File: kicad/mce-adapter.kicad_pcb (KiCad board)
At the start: 2 copper layers, 64.8 x 36.8 mm, 18 parts, among them U1 GAL16V8

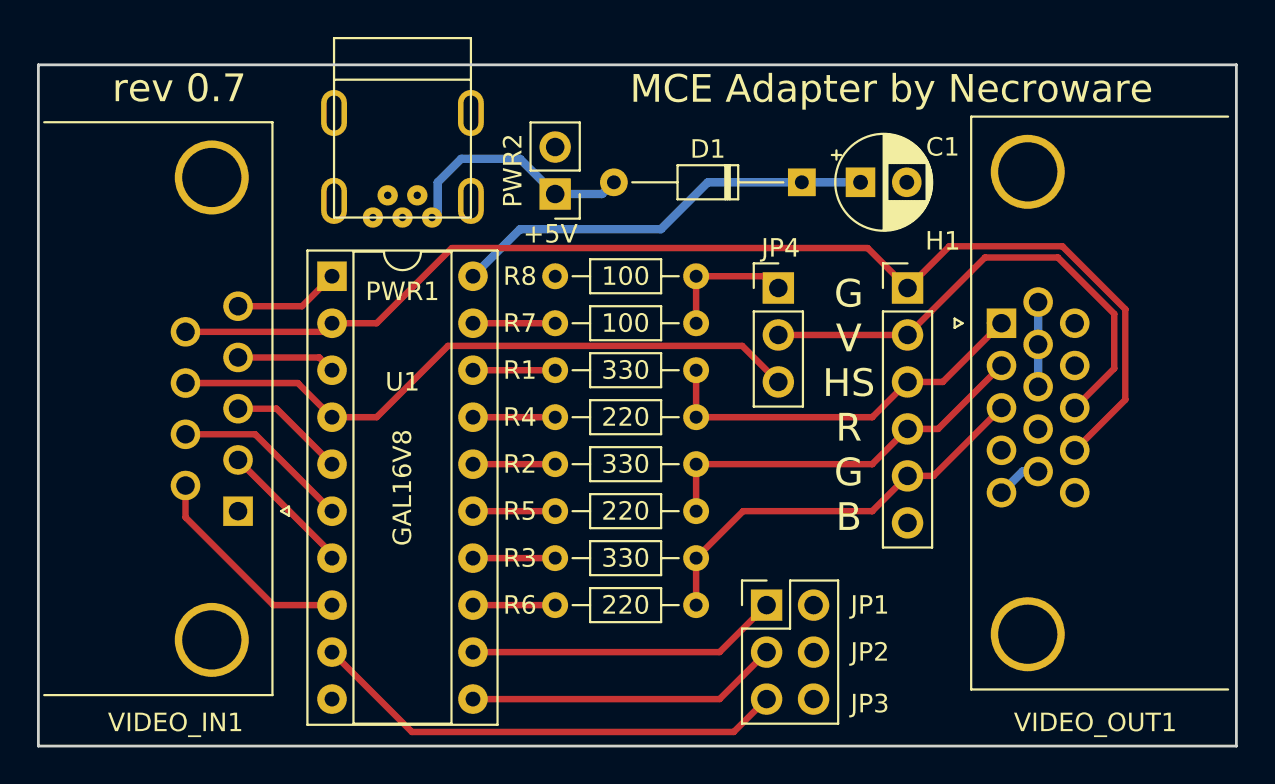
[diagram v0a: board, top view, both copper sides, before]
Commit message: Vastly shrink PCB
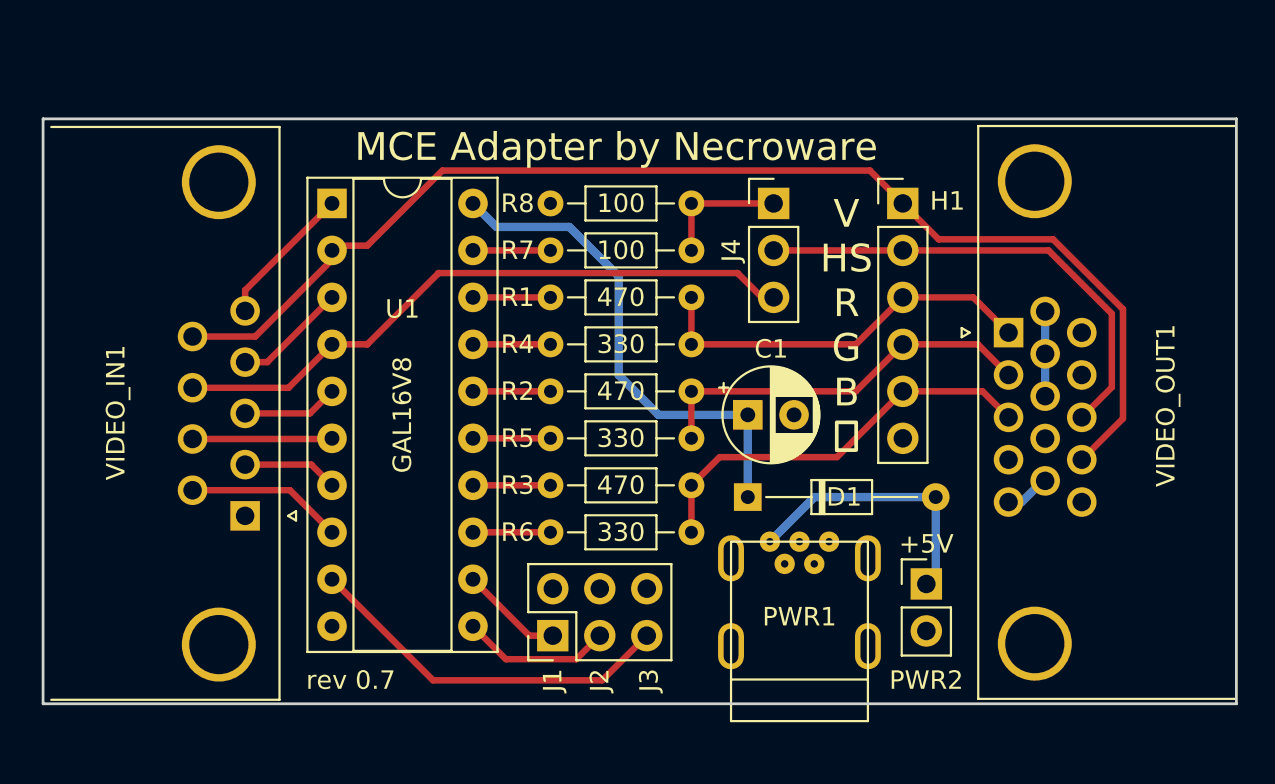
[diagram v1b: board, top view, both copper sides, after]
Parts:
- removed JP1-3: Conn_02x03_Odd_Even, Connector_PinHeader_2.54mm:PinHeader_2x03_P2.54mm_Vertical
- removed JP4: Conn_01x03_Male, Connector_PinHeader_2.54mm:PinHeader_1x03_P2.54mm_Vertical
- added J123: Conn_02x03_Odd_Even, Connector_PinHeader_2.54mm:PinHeader_2x03_P2.54mm_Vertical, F.Cu at (138.3, 114.7)
- added J4: Conn_01x03_Male, Connector_PinHeader_2.54mm:PinHeader_1x03_P2.54mm_Vertical, F.Cu at (150.2, 91.3)
- R1, R2, R3: value 330 -> 470
- R4, R5, R6: value 220 -> 330
- moved PWR2 29.1 mm to (158.5, 111.9), turned to 0 degrees
- moved PWR1 27.7 mm to (151.6, 109.6), turned to 0 degrees
- moved D1 17.3 mm to (148.8, 107.2), turned to 0 degrees
- moved C1 14.0 mm to (148.8, 102.7)
- moved H1 4.58 mm to (157.2, 91.3)
- moved R7 3.95 mm to (145.8, 93.9)
- moved R1 3.95 mm to (145.8, 96.4)
- moved R2 3.95 mm to (145.8, 101.5)
- moved R3 3.95 mm to (145.8, 106.6)
- moved R4 3.95 mm to (145.8, 98.9)
- moved R5 3.95 mm to (145.8, 104.0)
- moved R6 3.95 mm to (145.8, 109.1)
- moved R8 3.95 mm to (145.8, 91.3)
- moved U1 3.94 mm to (126.4, 91.3)
- moved VIDEO_OUT1 0.63 mm to (162.9, 98.3)
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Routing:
- net SW1_IN: track 16.9 -> 5.58 mm
- net SW2_IN: track 16.9 -> 8.12 mm
- net SW3_IN: track 26.0 -> 20.3 mm
- net Net-(C1-Pad1): track 23.1 -> 27.8 mm
- net IG_IN: track 11.6 -> 8.48 mm
- net Net-(D1-Pad2): track 13.1 -> 15.5 mm
- net IR_IN: track 7.41 -> 5.16 mm
- net IB_IN: track 9.78 -> 7.55 mm
- net B_IN: track 5.75 -> 7.76 mm
- net V_IN: track 65.0 -> 66.1 mm
- net R_IN: track 6.32 -> 5.19 mm
- net G_IN: track 5.37 -> 6.15 mm
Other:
- board size 64.8 x 36.8 mm -> 64.5 x 31.6 mm
- board text added: "V HS R G B ⏚"
- board text removed: "G V HS R G B"

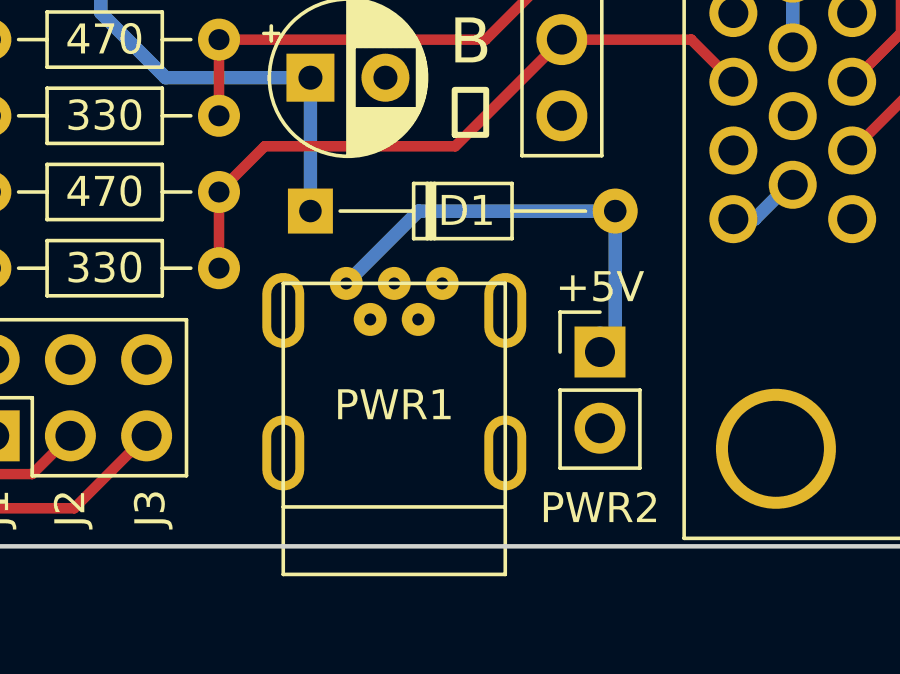
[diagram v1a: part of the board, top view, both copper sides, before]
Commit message: Move USB slightly over the edge
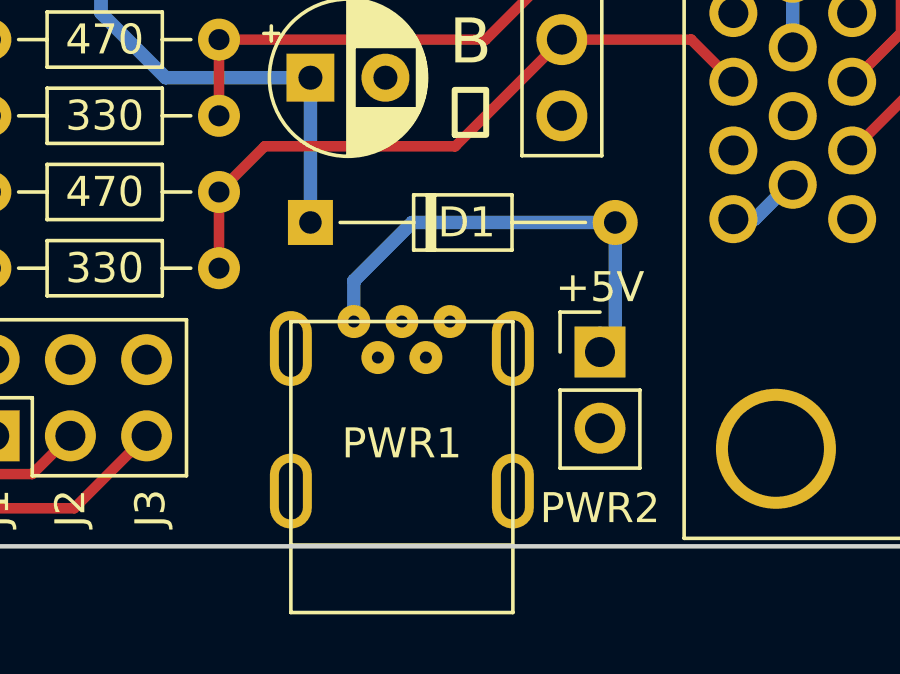
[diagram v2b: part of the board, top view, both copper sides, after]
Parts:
- moved PWR1 1.30 mm to (151.9, 110.9)
- moved D1 0.38 mm to (148.8, 107.6)
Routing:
- net Net-(D1-Pad2): track 15.5 -> 16.0 mm

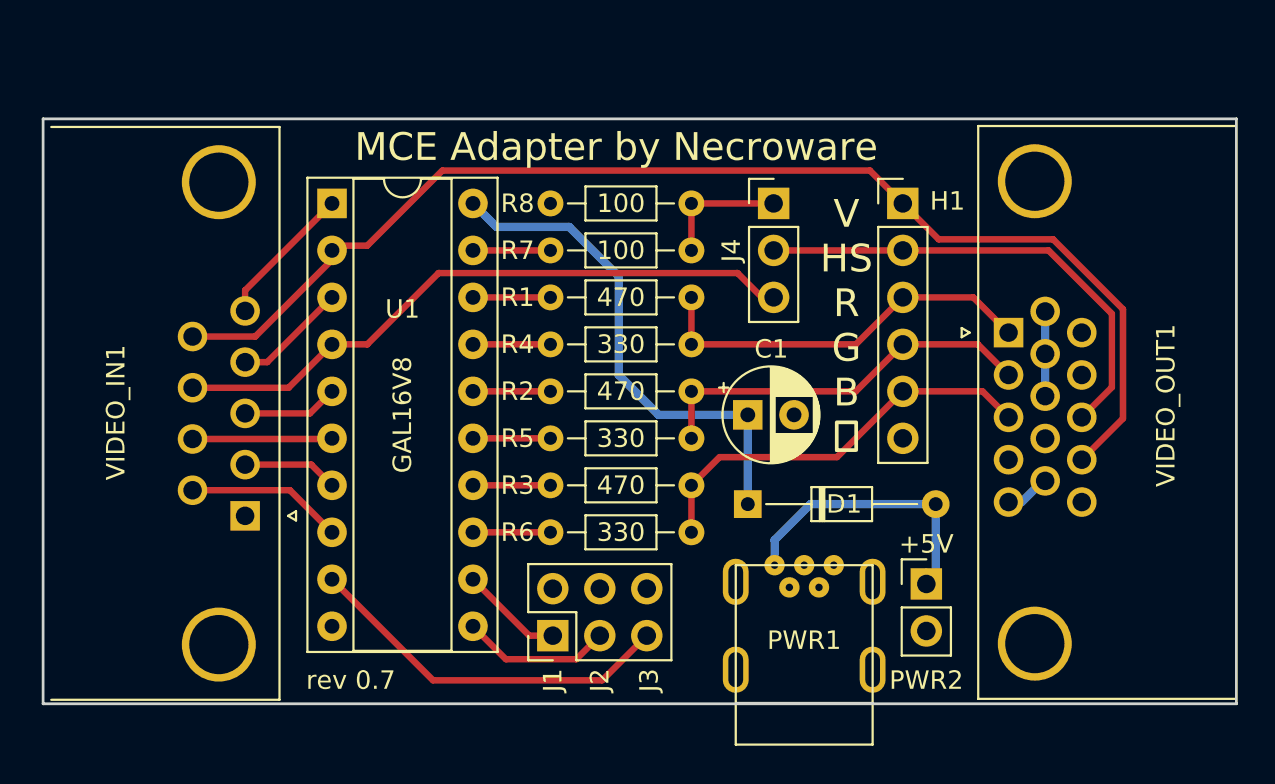
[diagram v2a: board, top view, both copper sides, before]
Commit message: Reajust some resistors improve layout
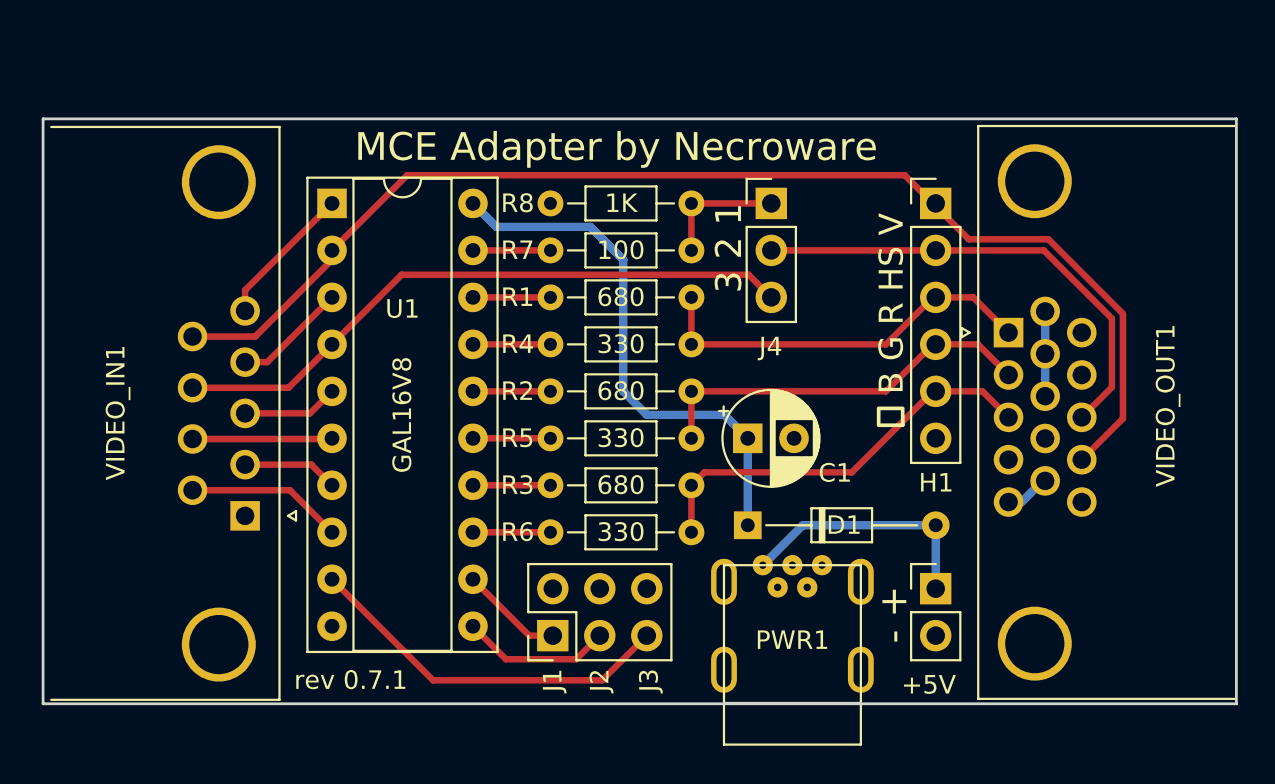
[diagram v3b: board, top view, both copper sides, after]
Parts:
- R1, R2, R3: value 470 -> 680
- R8: value 100 -> 1K
- moved H1 1.78 mm to (159.0, 91.3)
- moved C1 1.27 mm to (148.8, 104.0)
- moved D1 1.14 mm to (148.8, 108.7)
- moved PWR1 0.63 mm to (151.3, 110.9)
- moved PWR2 0.57 mm to (159.0, 112.1)
- moved J4 0.13 mm to (150.1, 91.3)
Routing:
- net Net-(D1-Pad2): track 16.0 -> 13.7 mm
- net Net-(C1-Pad1): track 27.8 -> 29.6 mm
- net H_OUT: track 27.2 -> 26.0 mm
- net R_OUT: track 22.2 -> 21.5 mm
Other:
- board text added: "rev 0.7.1"
- board text removed: "V HS R G B ⏚"
- board text removed: "rev 0.7"

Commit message: Move parts away from VGA out.
Add some back face silk notations
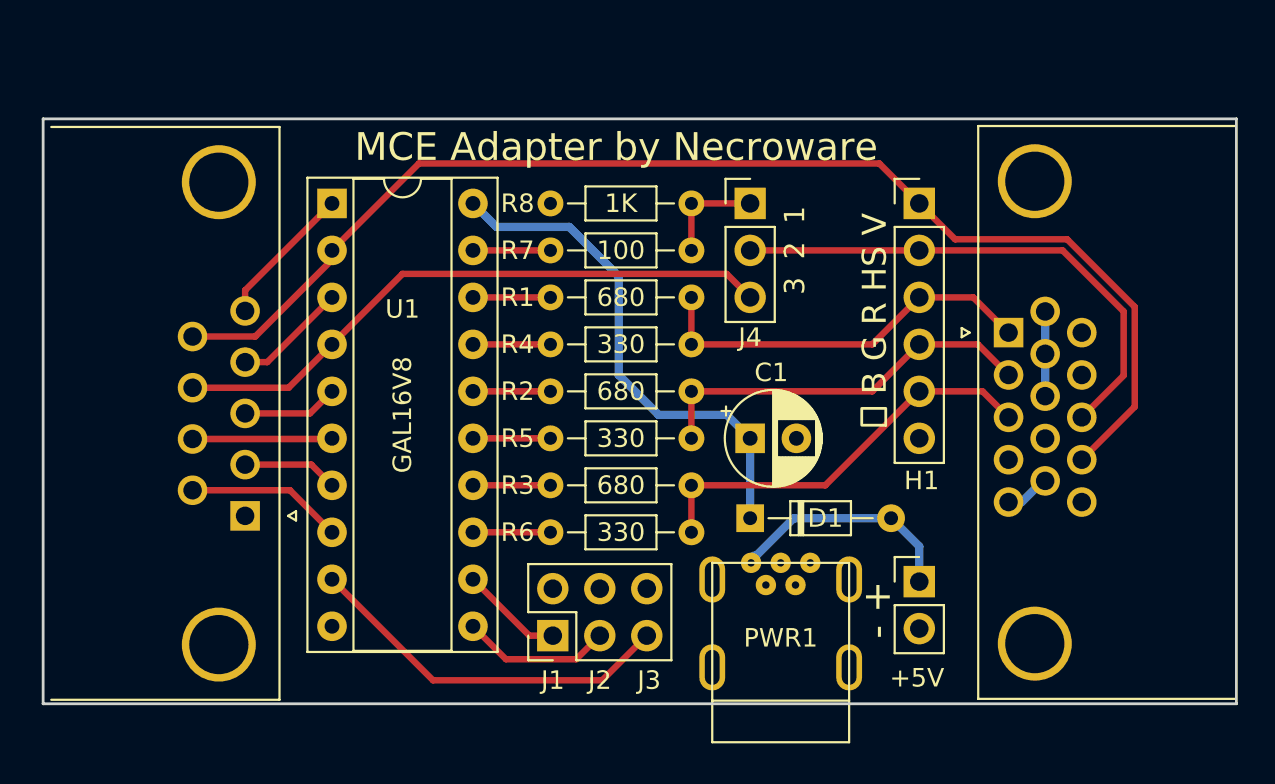
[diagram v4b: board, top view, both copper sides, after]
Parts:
- D1: footprint Diode_THT:D_DO-34_SOD68_P10.16mm_Horizontal -> Diode_THT:D_DO-34_SOD68_P7.62mm_Horizontal
- moved J4 1.14 mm to (149.0, 91.3)
- moved PWR2 0.97 mm to (158.1, 111.8)
- moved H1 0.89 mm to (158.1, 91.3)
- moved PWR1 0.65 mm to (150.6, 110.7)
- moved D1 0.40 mm to (149.0, 108.3)
- moved C1 0.13 mm to (149.0, 104.0)
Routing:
- net H_OUT: track 26.0 -> 28.2 mm
- net Net-(C1-Pad1): track 29.6 -> 27.7 mm
- net V_IN: track 66.1 -> 67.8 mm
- net Net-(D1-Pad2): track 13.7 -> 12.3 mm
- net S_OUT: track 6.86 -> 5.72 mm
- net H_IN: track 34.3 -> 33.2 mm
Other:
- board text added: "J1: color/mono J2: mode select"
- board text added: "J3: invert sync J4: sync S:1-2 H:2-3"
